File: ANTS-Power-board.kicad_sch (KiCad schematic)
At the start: 0 parts

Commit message: add capacitor
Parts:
- added C?: 1u, symbol Device:C
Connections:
- new net +3.3V: C?.1
- new net GND: C?.2
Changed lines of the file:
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@@
 	(generator_version "9.0")
 	(paper "A4")
+	(symbol
+		(lib_id "power:GND")
+		(at 132.08 95.25 0)
+		(unit 1)
+		(exclude_from_sim no)
+		(in_bom yes)
+		(on_board yes)
+		(dnp no)
+		(fields_autoplaced yes)
+		(property "Reference" "#PWR02"
+			(at 132.08 101.6 0)
+			(effects
+				(font
+					(size 1.27 1.27)
+				)
+				(hide yes)
+			)
+		)
+		(property "Value" "GND"
+			(at 132.08 100.33 0)
+			(effects
+				(font
+					(size 1.27 1.27)
+				)
+			)
+		)
+		(property "Footprint" ""
+			(at 132.08 95.25 0)
+			(effects
+				(font
+					(size 1.27 1.27)
+				)
+				(hide yes)
+			)
+		)
+		(property "Datasheet" ""
+			(at 132.08 95.25 0)
+			(effects
+				(font
+					(size 1.27 1.27)
+				)
+				(hide yes)
+			)
+		)
+		(property "Description" "Power symbol creates a global label with name \"GND\" , ground"
+			(at 132.08 95.25 0)
+			(effects
+				(font
+					(size 1.27 1.27)
+				)
+				(hide yes)
+			)
+		)
+		(pin "1"
+		)
+		(instances
+			(project ""
+				(path "/4d632659-7d2f-4407-ada5-b4e72f7be845"
+					(reference "#PWR02")
+					(unit 1)
+				)
+			)
+		)
+	)
+	(symbol
+		(lib_id "power:+3.3V")
+		(at 132.08 87.63 0)
+		(unit 1)
+		(exclude_from_sim no)
+		(in_bom yes)
+		(on_board yes)
+		(dnp no)
+		(fields_autoplaced yes)
+		(property "Reference" "#PWR01"
+			(at 132.08 91.44 0)
+			(effects
+				(font
+					(size 1.27 1.27)
+				)
+				(hide yes)
+			)
+		)
+		(property "Value" "+3.3V"
+			(at 132.08 82.55 0)
+			(effects
+				(font
+					(size 1.27 1.27)
+				)
+			)
+		)
+		(property "Footprint" ""
+			(at 132.08 87.63 0)
+			(effects
+				(font
+					(size 1.27 1.27)
+				)
+				(hide yes)
+			)
+		)
+		(property "Datasheet" ""
+			(at 132.08 87.63 0)
+			(effects
+				(font
+					(size 1.27 1.27)
+				)
+				(hide yes)
+			)
+		)
+		(property "Description" "Power symbol creates a global label with name \"+3.3V\""
+			(at 132.08 87.63 0)
+			(effects
+				(font
+					(size 1.27 1.27)
+				)
+				(hide yes)
+			)
+		)
+		(pin "1"
+		)
+		(instances
+			(project ""
+				(path "/4d632659-7d2f-4407-ada5-b4e72f7be845"
+					(reference "#PWR01")
+					(unit 1)
+				)
+			)
+		)
+	)
+	(symbol
+		(lib_id "Device:C")
+		(at 132.08 91.44 0)
+		(unit 1)
+		(exclude_from_sim no)
+		(in_bom yes)
+		(on_board yes)
+		(dnp no)
+		(fields_autoplaced yes)
+		(property "Reference" "C?"
+			(at 135.89 90.1699 0)
+			(effects
+				(font
+					(size 1.27 1.27)
+				)
+				(justify left)
+			)
+		)
+		(property "Value" "1u"
+			(at 135.89 92.7099 0)
+			(effects
+				(font
+					(size 1.27 1.27)
+				)
+				(justify left)
+			)
+		)
+		(property "Footprint" ""
+			(at 133.0452 95.25 0)
+			(effects
+				(font
+					(size 1.27 1.27)
+				)
+				(hide yes)
+			)
+		)
+		(property "Datasheet" "~"
+			(at 132.08 91.44 0)
+			(effects
+				(font
+					(size 1.27 1.27)
+				)
+				(hide yes)
+			)
+		)
+		(property "Description" "Unpolarized capacitor"
+			(at 132.08 91.44 0)
+			(effects
+				(font
+					(size 1.27 1.27)
+				)
+				(hide yes)
+			)
+		)
+		(pin "1"
+		)
+		(pin "2"
+		)
+		(instances
+			(project ""
+				(path "/4d632659-7d2f-4407-ada5-b4e72f7be845"
+					(reference "C?")
+					(unit 1)
+				)
+			)
+		)
+	)
 	(sheet_instances
 		(path "/"

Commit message: Initial Project and Components creation
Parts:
- removed C?: 1u, symbol Device:C
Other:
- added sheet 3.3v_LDO (3.3v_LDO.kicad_sch)
- added sheet 5V SMPS (5v_smps.kicad_sch)
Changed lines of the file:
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@@
 	(generator_version "9.0")
 	(paper "A4")
-	(symbol
-		(lib_id "power:GND")
-		(at 132.08 95.25 0)
-		(unit 1)
+	(sheet
+		(at 67.31 132.08)
+		(size 27.94 19.05)
 		(exclude_from_sim no)
 		(in_bom yes)
@@
 		(dnp no)
 		(fields_autoplaced yes)
-		(property "Reference" "#PWR02"
-			(at 132.08 101.6 0)
+		(stroke
+			(width 0.1524)
+			(type solid)
+		)
+		(fill
+			(color 0 0 0 0.0000)
+		)
+		(property "Sheetname" "3.3v_LDO"
+			(at 67.31 131.3684 0)
 			(effects
 				(font
 					(size 1.27 1.27)
 				)
-				(hide yes)
+				(justify left bottom)
 			)
 		)
-		(property "Value" "GND"
-			(at 132.08 100.33 0)
+		(property "Sheetfile" "3.3v_LDO.kicad_sch"
+			(at 67.31 151.7146 0)
 			(effects
 				(font
 					(size 1.27 1.27)
 				)
+				(justify left top)
 			)
 		)
-		(property "Footprint" ""
-			(at 132.08 95.25 0)
-			(effects
-				(font
-					(size 1.27 1.27)
-				)
-				(hide yes)
-			)
-		)
-		(property "Datasheet" ""
-			(at 132.08 95.25 0)
-			(effects
-				(font
-					(size 1.27 1.27)
-				)
-				(hide yes)
-			)
-		)
-		(property "Description" "Power symbol creates a global label with name \"GND\" , ground"
-			(at 132.08 95.25 0)
-			(effects
-				(font
-					(size 1.27 1.27)
-				)
-				(hide yes)
-			)
-		)
-		(pin "1"
-		)
 		(instances
-			(project ""
+			(project "ANTS-Power-board"
 				(path "/4d632659-7d2f-4407-ada5-b4e72f7be845"
-					(reference "#PWR02")
-					(unit 1)
+					(page "3")
 				)
 			)
 		)
 	)
-	(symbol
-		(lib_id "power:+3.3V")
-		(at 132.08 87.63 0)
-		(unit 1)
+	(sheet
+		(at 26.67 132.08)
+		(size 31.75 19.05)
 		(exclude_from_sim no)
 		(in_bom yes)
@@
 		(dnp no)
 		(fields_autoplaced yes)
-		(property "Reference" "#PWR01"
-			(at 132.08 91.44 0)
+		(stroke
+			(width 0.1524)
+			(type solid)
+		)
+		(fill
+			(color 0 0 0 0.0000)
+		)
+		(property "Sheetname" "5V SMPS"
+			(at 26.67 131.3684 0)
 			(effects
 				(font
 					(size 1.27 1.27)
 				)
-				(hide yes)
+				(justify left bottom)
 			)
 		)
-		(property "Value" "+3.3V"
-			(at 132.08 82.55 0)
+		(property "Sheetfile" "5v_smps.kicad_sch"
+			(at 26.67 151.7146 0)
 			(effects
 				(font
 					(size 1.27 1.27)
 				)
+				(justify left top)
 			)
 		)
-		(property "Footprint" ""
-			(at 132.08 87.63 0)
-			(effects
-				(font
-					(size 1.27 1.27)
-				)
-				(hide yes)
-			)
-		)
-		(property "Datasheet" ""
-			(at 132.08 87.63 0)
-			(effects
-				(font
-					(size 1.27 1.27)
-				)
-				(hide yes)
-			)
-		)
-		(property "Description" "Power symbol creates a global label with name \"+3.3V\""
-			(at 132.08 87.63 0)
-			(effects
-				(font
-					(size 1.27 1.27)
-				)
-				(hide yes)
-			)
-		)
-		(pin "1"
-		)
 		(instances
-			(project ""
+			(project "ANTS-Power-board"
 				(path "/4d632659-7d2f-4407-ada5-b4e72f7be845"
-					(reference "#PWR01")
-					(unit 1)
+					(page "2")
 				)
 			)
-		)
-	)
-	(symbol
-		(lib_id "Device:C")
-		(at 132.08 91.44 0)
-		(unit 1)
-		(exclude_from_sim no)
-		(in_bom yes)
-		(on_board yes)
-		(dnp no)
-		(fields_autoplaced yes)
-		(property "Reference" "C?"
-			(at 135.89 90.1699 0)
-			(effects
-				(font
-					(size 1.27 1.27)
-				)
-				(justify left)
-			)
-		)
-		(property "Value" "1u"
-			(at 135.89 92.7099 0)
-			(effects
-				(font
-					(size 1.27 1.27)
-				)
-				(justify left)
-			)
-		)
-		(property "Footprint" ""
-			(at 133.0452 95.25 0)
-			(effects
-				(font
-					(size 1.27 1.27)
-				)
-				(hide yes)
-			)
-		)
-		(property "Datasheet" "~"
-			(at 132.08 91.44 0)
-			(effects
-				(font
-					(size 1.27 1.27)
-				)
-				(hide yes)
-			)
-		)
-		(property "Description" "Unpolarized capacitor"
-			(at 132.08 91.44 0)
-			(effects
-				(font
-					(size 1.27 1.27)
-				)
-				(hide yes)
-			)
-		)
-		(pin "1"
-		)
-		(pin "2"
-		)
-		(instances
-			(project ""
-				(path "/4d632659-7d2f-4407-ada5-b4e72f7be845"
-					(reference "C?")
-					(unit 1)
-				)
-			)

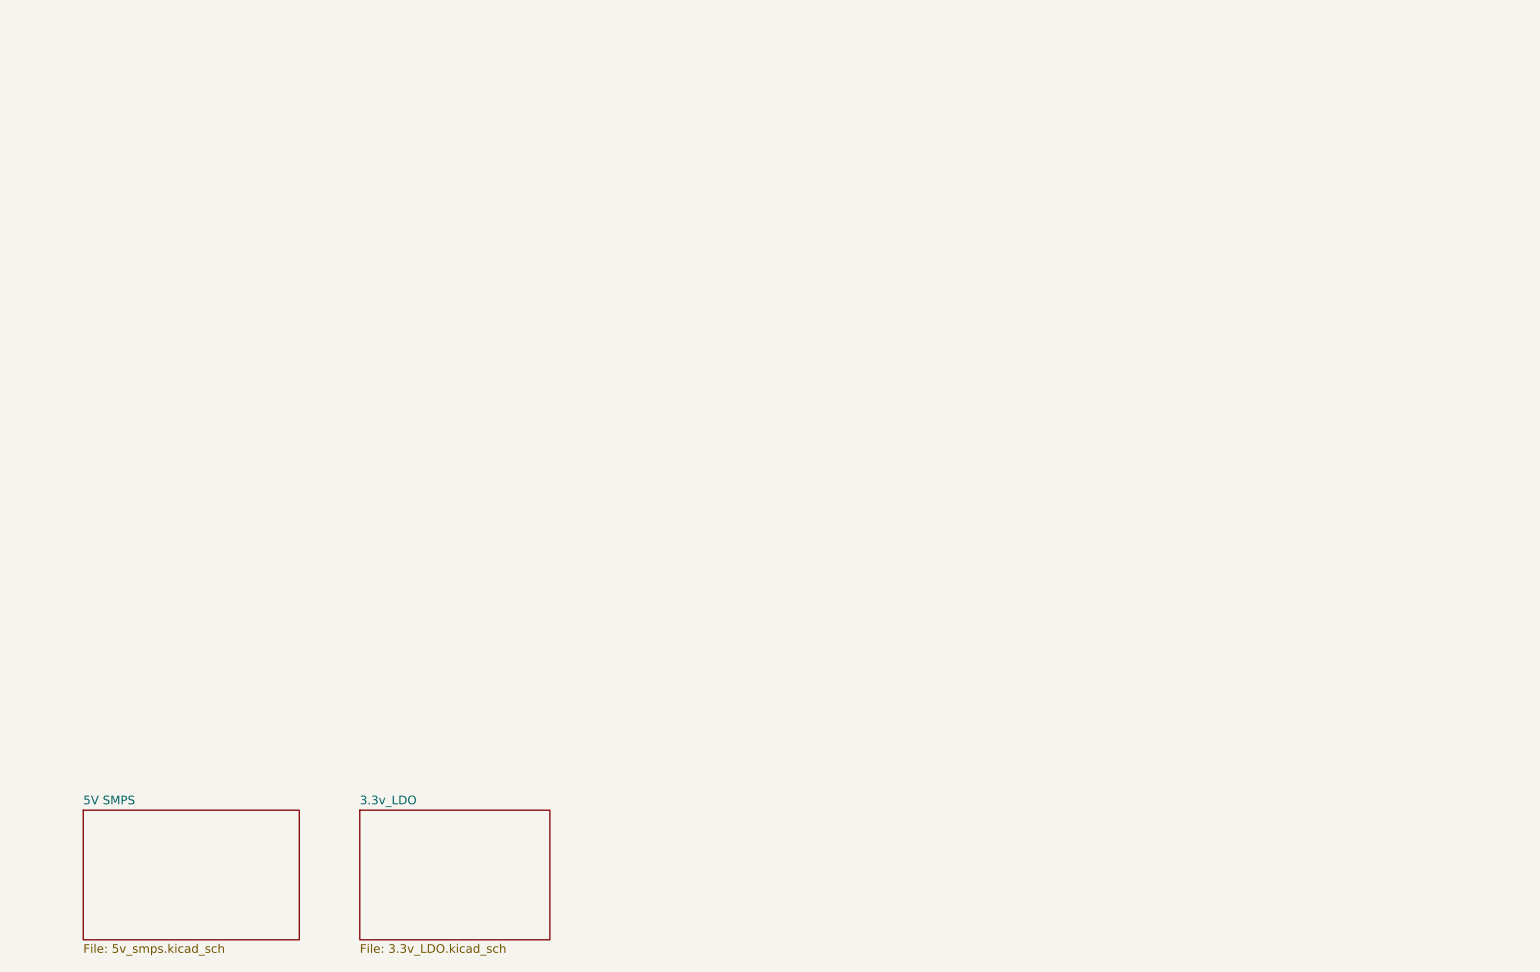
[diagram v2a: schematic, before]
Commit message: updated smps
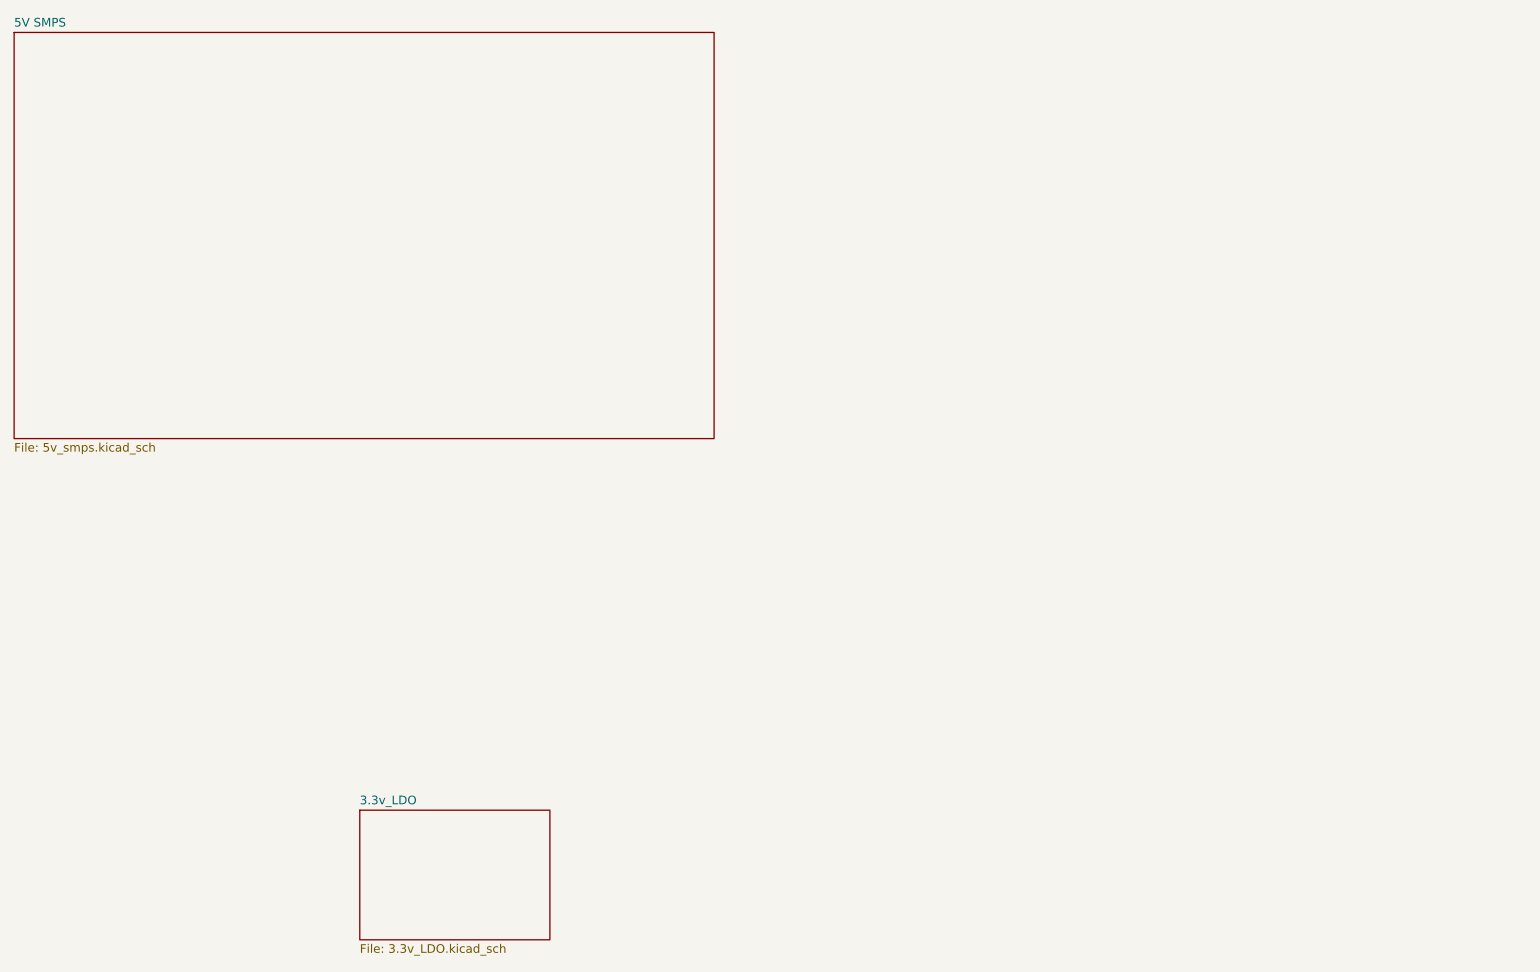
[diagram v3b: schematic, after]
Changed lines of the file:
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@@
 	)
 	(sheet
-		(at 26.67 132.08)
-		(size 31.75 19.05)
+		(at 16.51 17.78)
+		(size 102.87 59.69)
 		(exclude_from_sim no)
 		(in_bom yes)
@@
 		)
 		(property "Sheetname" "5V SMPS"
-			(at 26.67 131.3684 0)
+			(at 16.51 17.0684 0)
 			(effects
 				(font
@@
 		)
 		(property "Sheetfile" "5v_smps.kicad_sch"
-			(at 26.67 151.7146 0)
+			(at 16.51 78.0546 0)
 			(effects
 				(font

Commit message: Ross Added branch
added a branch
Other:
- added sheet 3.3V_LDO (3.3v_LDO.kicad_sch)
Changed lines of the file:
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@@
+	)
+	(sheet
+		(at 209.55 76.2)
+		(size 12.7 3.81)
+		(exclude_from_sim no)
+		(in_bom yes)
+		(on_board yes)
+		(dnp no)
+		(fields_autoplaced yes)
+		(stroke
+			(width 0.1524)
+			(type solid)
+		)
+		(fill
+			(color 0 0 0 0.0000)
+		)
+		(property "Sheetname" "3.3V_LDO"
+			(at 209.55 75.4884 0)
+			(effects
+				(font
+					(size 1.27 1.27)
+				)
+				(justify left bottom)
+			)
+		)
+		(property "Sheetfile" "3.3v_LDO.kicad_sch"
+			(at 209.55 80.5946 0)
+			(effects
+				(font
+					(size 1.27 1.27)
+				)
+				(justify left top)
+			)
+		)
+		(instances
+			(project "ANTS-Power-board"
+				(path "/4d632659-7d2f-4407-ada5-b4e72f7be845"
+					(page "4")
+				)
+			)
+		)
 	)
 	(sheet
